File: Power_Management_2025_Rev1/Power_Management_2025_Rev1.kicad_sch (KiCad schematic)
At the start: 101 parts, among them J1 RJ45_LED_Shielded, Q1 BSS138, Q2 IPB180N10S4-02, Q3 IPB180N10S4-02, Q4 IPB180N10S4-02, U1 Teensy4.1_DEV-16771, U10 LT1910, U11 LT1910, U12 PKE3316ZPI, U13 PKE3316ZPI, U14 LT1910, U2 OKI-78SR-3.3_1.5-W36-C, U3 ACS756xCB-050B-PFF, U4 ${SIM.PARAMS}, U5 ${SIM.PARAMS}, U6 ${SIM.PARAMS}, U7 ${SIM.PARAMS}, U8 ${SIM.PARAMS}, U9 ${SIM.PARAMS}

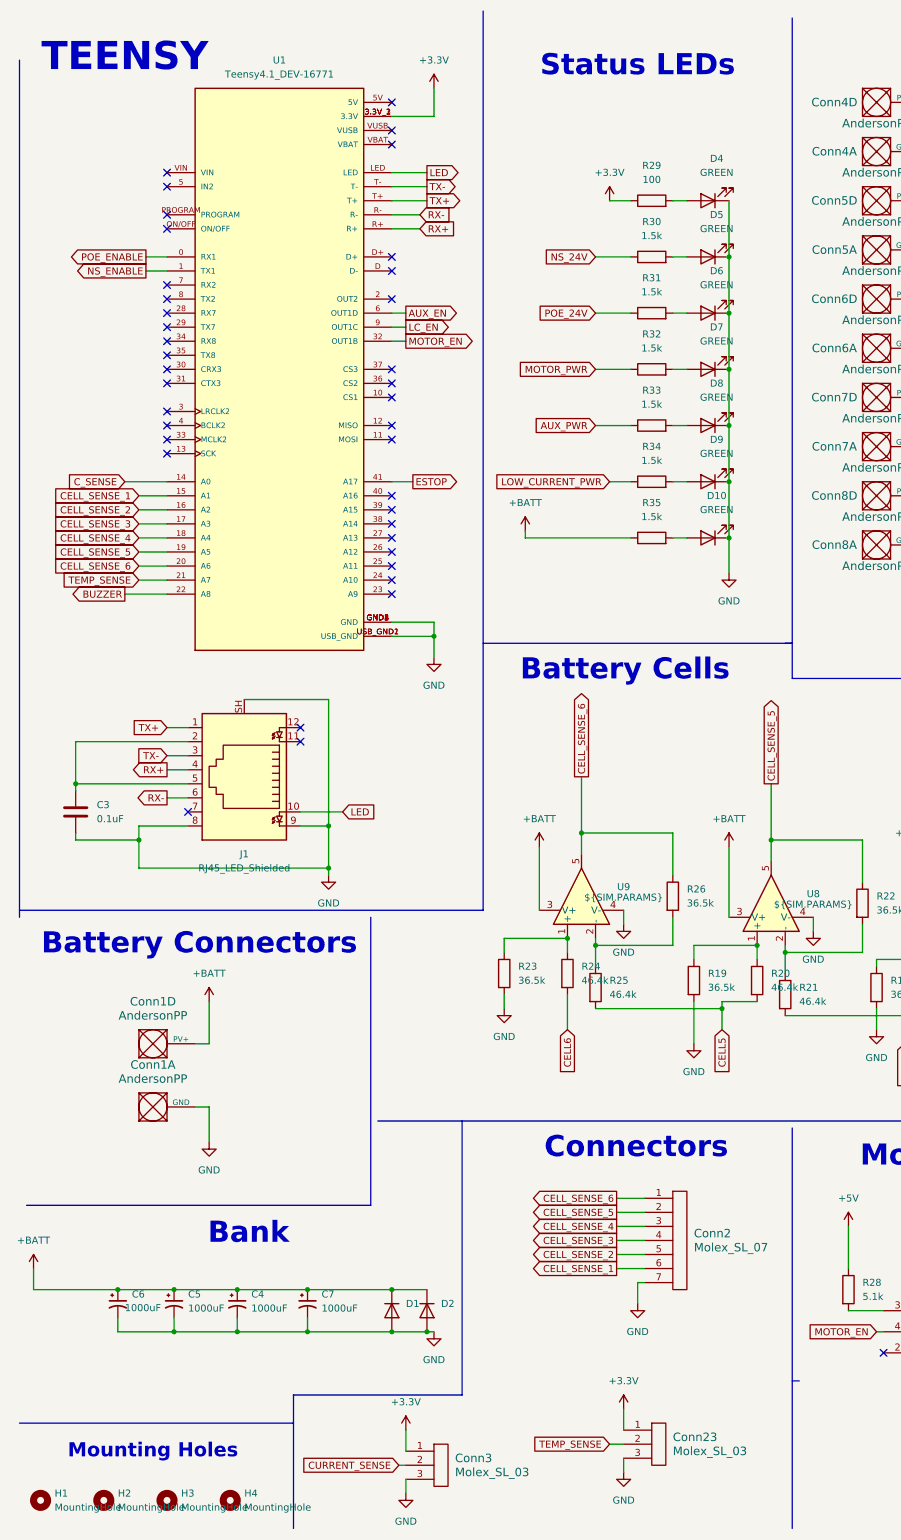
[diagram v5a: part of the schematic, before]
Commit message: Finished reverse voltage protection circuit
The reverse voltage protection circuit was finished with a shottky diode, and a PTC fuse. Then an additional set of current sensing wires and battery voltage andersons were also placed for smart battery
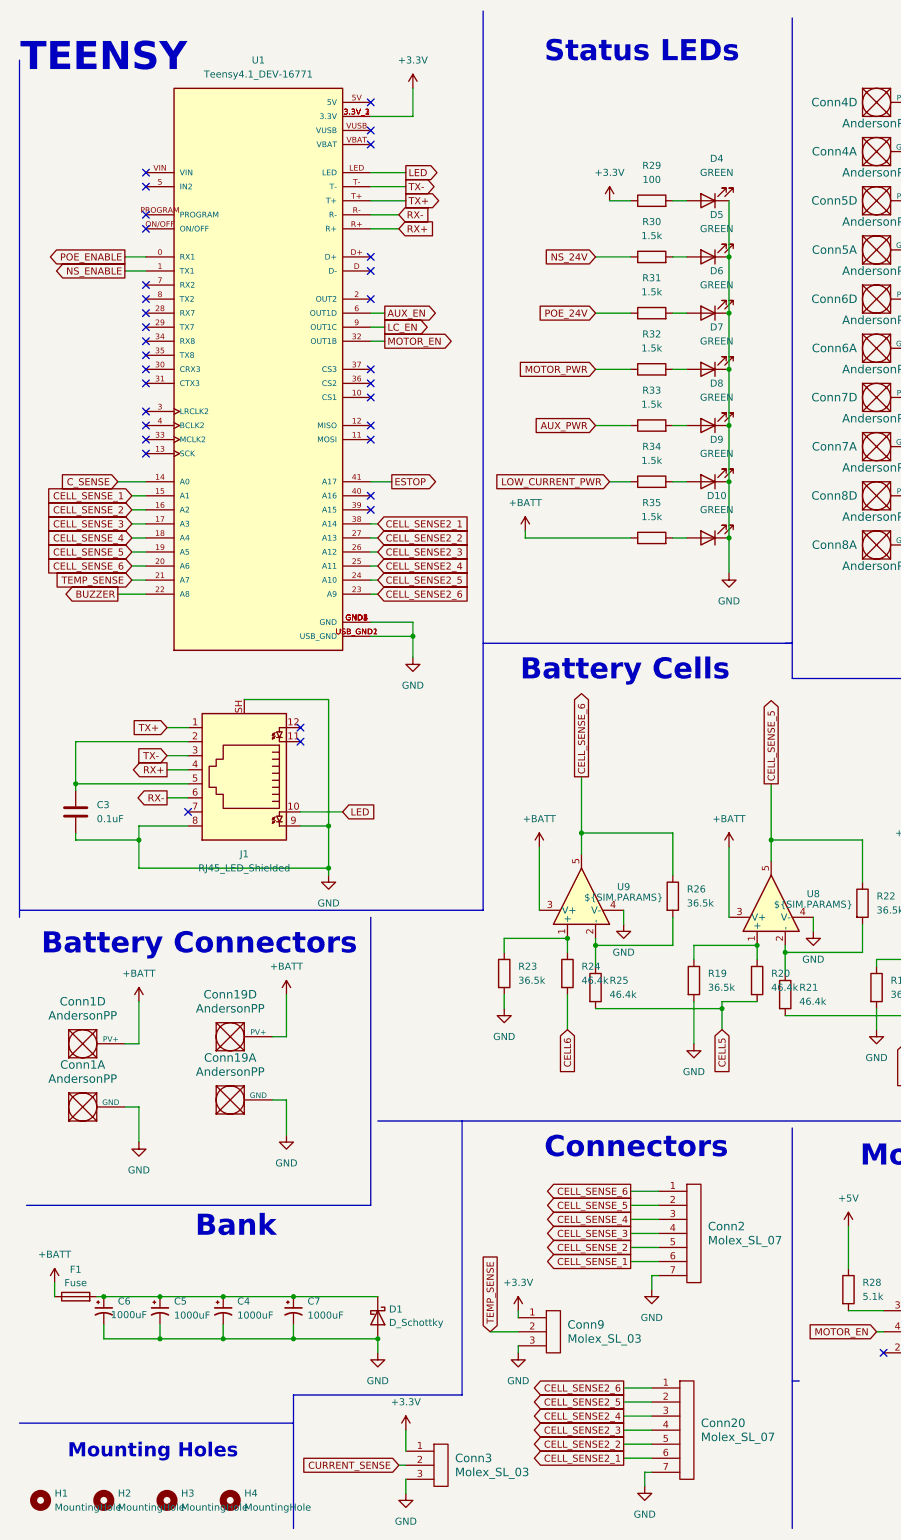
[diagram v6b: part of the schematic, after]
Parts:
- removed Conn23: Molex_SL_03, symbol MRDT_Connectors:Molex_SL_03
- removed D1, D2: ~, symbol Device:D
- added Conn19: AndersonPP, symbol MRDT_Connectors:AndersonPP
- added Conn20: Molex_SL_07, symbol MRDT_Connectors:Molex_SL_07
- added Conn9: Molex_SL_03, symbol MRDT_Connectors:Molex_SL_03
- added D1: D_Schottky, symbol Device:D_Schottky
- added F1: Fuse, symbol Device:Fuse
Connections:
- net +3.3V: now also Conn9.1
- net +BATT: now also Conn19.4 (PV+), F1.1; no longer C4.1, C5.1, C6.1, C7.1
- net GND: now also Conn19.1 (GND), Conn20.7, Conn9.3, D1.2 (A)
- net TEMP_SENSE: now also Conn9.2
- net CELL_SENSE2_6: now reaches U1.23 (A9)
- net CELL_SENSE2_6: now also Conn20.1
- net CELL_SENSE2_5: now reaches U1.24 (A10)
- net CELL_SENSE2_5: now also Conn20.2
- net CELL_SENSE2_4: now reaches U1.25 (A11)
- net CELL_SENSE2_4: now also Conn20.3
- net CELL_SENSE2_3: now reaches U1.26 (A12)
- net CELL_SENSE2_3: now also Conn20.4
- net CELL_SENSE2_2: now reaches U1.27 (A13)
- net CELL_SENSE2_2: now also Conn20.5
- net CELL_SENSE2_1: now reaches U1.38 (A14)
- net CELL_SENSE2_1: now also Conn20.6
- new net: C4.1, C5.1, C6.1, C7.1, D1.1 (K), F1.2
- no-connect marks 43 -> 37
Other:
- moved on the sheet: C4, C5, C6, C7, Conn1A, Conn1D, Conn2, U1

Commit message: Footprint assignments
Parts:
- B1: footprint (none) -> Buzzer_Beeper:Buzzer_12x9.5RM7.6
- C1, C11, C12, C13, C14, C2, C9: footprint (none) -> Capacitor_THT:CP_Radial_D5.0mm_P2.00mm
- C10, C8: footprint (none) -> Capacitor_THT:CP_Radial_Tantal_D5.0mm_P5.00mm
- C3: footprint (none) -> Capacitor_SMD:C_0603_1608Metric_Pad1.08x0.95mm_HandSolder
- C4, C5, C6, C7: footprint (none) -> Capacitor_THT:CP_Radial_D16.0mm_P7.50mm
- Conn1, Conn19: footprint (none) -> MRDT_Connectors:Anderson_1_Horizontal
- Conn10, Conn11, Conn12, Conn13, Conn14, Conn15, Conn16, Conn17, Conn18: footprint MRDT_Connectors:Square_Anderson_2_H_Stacked -> MRDT_Connectors:Anderson_1_Horizontal
- Conn2, Conn20: footprint (none) -> MRDT_Connectors:MOLEX_SL_07_Horizontal
- Conn3, Conn9: footprint (none) -> MRDT_Connectors:MOLEX_SL_03_Horizontal
- D1: footprint (none) -> Package_TO_SOT_SMD:TO-263-2_TabPin1
- D10, D3, D4, D5, D6, D7, D8, D9: footprint (none) -> Diode_SMD:D_0603_1608Metric_Pad1.05x0.95mm_HandSolder
- F1: footprint (none) -> KiCad:3140167
- H1, H2, H3, H4: footprint (none) -> MRDT_Drill_Holes:4_40_Hole_Corner
- J1: footprint (none) -> MRDT_Connectors:RJ45_Teensy
- R1, R10, R11, R12, R13, R14, R15, R16, R17, R18, R19, R2, R20, R21, R22, R23, R24, R25, R26, R27, R28, R29, R3, R30, R31, R32, R33, R34, R35, R4, R5, R6, R7, R8, R9: footprint (none) -> Resistor_SMD:R_0603_1608Metric_Pad0.98x0.95mm_HandSolder
- U1: footprint MODULE_DEV-16771 -> MRDT_Shields:Teensy_4_1_Ethernet
- U10, U11, U14: footprint (none) -> Package_SO:SOIC-8-N7_3.9x4.9mm_P1.27mm
- U12, U13: footprint (none) -> MRDT_Devices:PKE3316ZPI
- U4, U5, U6, U7, U8, U9: footprint (none) -> Package_SO:SOIC-8_3.9x4.9mm_P1.27mm

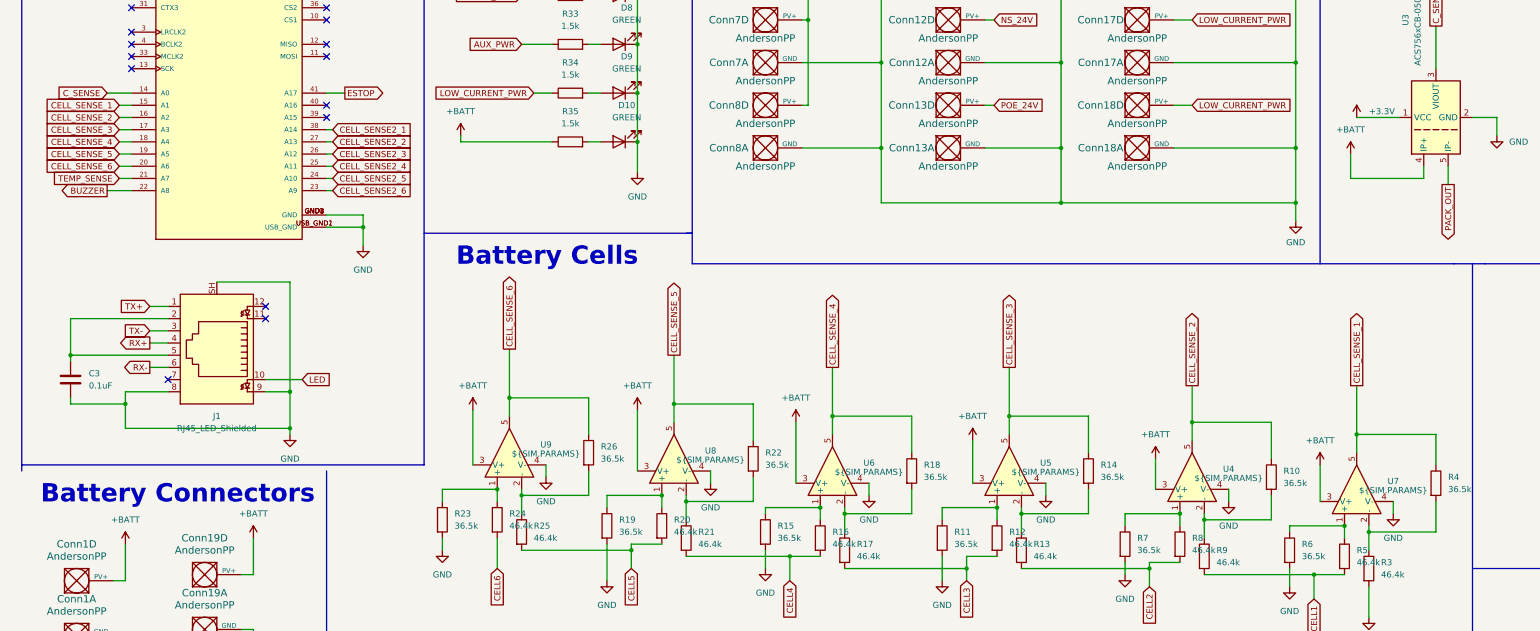
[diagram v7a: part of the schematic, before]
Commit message: Started on PCB editor
Started layout grouped components began trace work
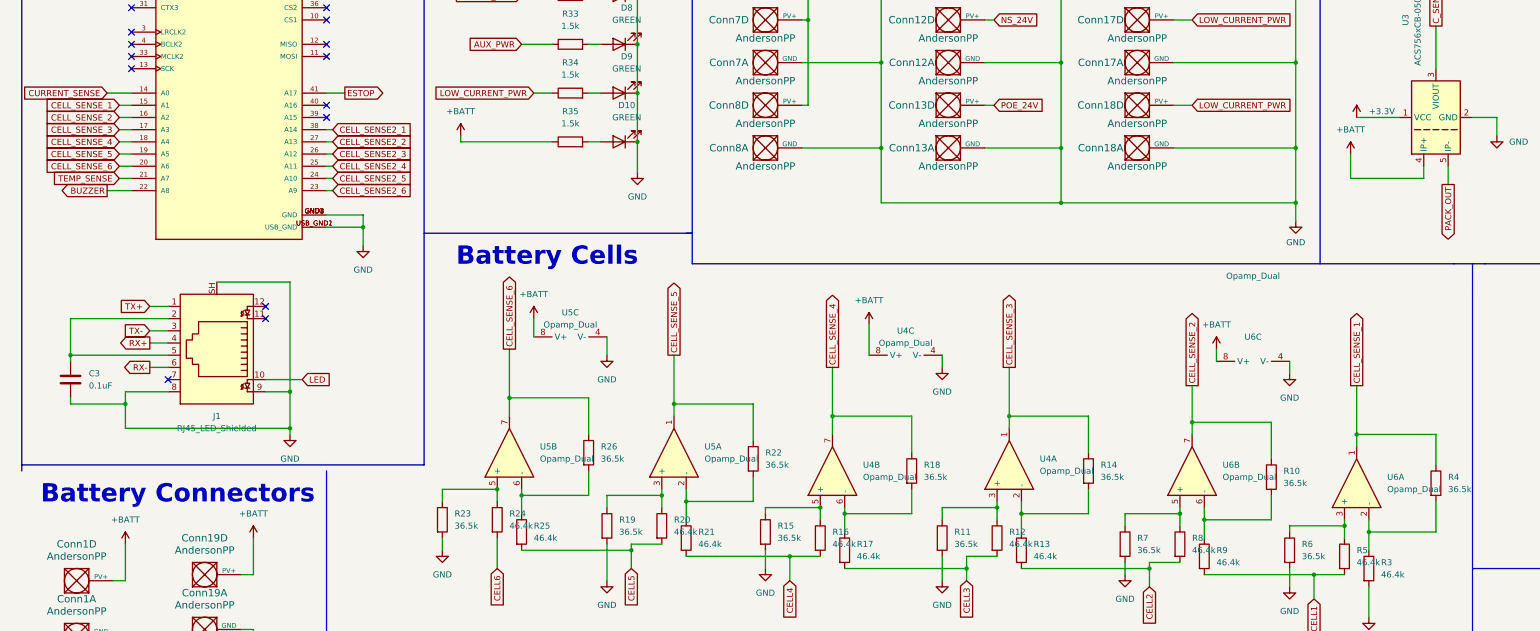
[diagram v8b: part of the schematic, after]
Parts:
- removed U4, U5, U6, U7, U8, U9: ${SIM.PARAMS}, Package_SO:SOIC-8_3.9x4.9mm_P1.27mm, symbol Simulation_SPICE:OPAMP
- added U4, U5, U6: Opamp_Dual, Package_SO:SO-8_3.9x4.9mm_P1.27mm, symbol Device:Opamp_Dual
- Conn1, Conn10, Conn11, Conn12, Conn13, Conn14, Conn15, Conn16, Conn17, Conn18, Conn19: footprint MRDT_Connectors:Anderson_1_Horizontal -> MRDT_Connectors:Square_Anderson_2_H_Side_By_Side_PV
- Conn4, Conn5, Conn6, Conn7, Conn8: footprint MRDT_Connectors:Square_Anderson_2_H_Stacked -> MRDT_Connectors:Square_Anderson_2_H_Side_By_Side_PV
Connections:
- net +BATT: now also U4.8 (V+), U5.8 (V+), U6.8 (V+)
- net CELL_SENSE_1: now also U6.1
- net CELL_SENSE_2: now also U6.7
- net CELL_SENSE_3: now also U4.1
- net CELL_SENSE_4: now also U4.7
- net CELL_SENSE_5: now also U5.1
- net CELL_SENSE_6: now also U5.7
- net CURRENT_SENSE: now also U1.14 (A0)
- net C_SENSE: no longer U1.14 (A0)
- net GND: now also U4.4 (V-), U5.4 (V-), U6.4 (V-)
- net at R11.1, R12.1: now also U4.3 (+)
- net at R10.2, R9.1: now also U6.6 (-)
- net at R5.1, R6.1: now also U6.3 (+)
- net at R3.1, R4.2: now also U6.2 (-)
- net at R25.1, R26.2: now also U5.6 (-)
- net at R7.1, R8.1: now also U6.5 (+)
- net at R17.1, R18.2: now also U4.6 (-)
- net at R19.1, R20.1: now also U5.3 (+)
- net at R21.1, R22.2: now also U5.2 (-)
- net at R23.1, R24.1: now also U5.5 (+)
- net at R15.1, R16.1: now also U4.5 (+)
- net at R13.1, R14.2: now also U4.2 (-)
